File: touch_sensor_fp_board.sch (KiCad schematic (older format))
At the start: 18 parts, among them P1 Touch Sensor, P2 Touch Sensor, P3 Touch Sensor, U1 ttp223-ba6, U2 ttp223-ba6, U3 ttp223-ba6

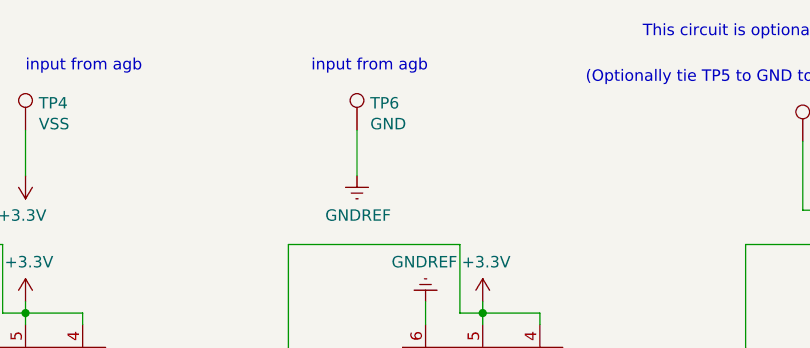
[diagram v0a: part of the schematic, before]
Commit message: updated wording on schematic
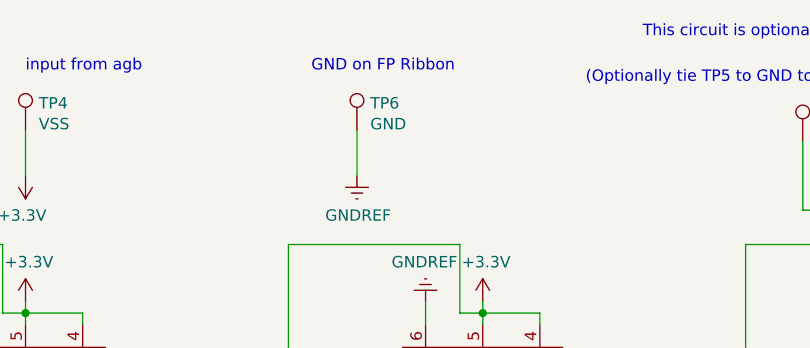
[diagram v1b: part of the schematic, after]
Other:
- note added: "GND on FP Ribbon"
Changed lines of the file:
@@
 input from agb
 Text Notes 5150 2800 0    50   ~ 0
-input from agb
+GND on FP Ribbon
 Text Notes 6350 2850 0    50   ~ 0
 (Optionally tie TP5 to GND to not use a third togglable touch sensor, only do this if you dont populate the IC's footprint)
